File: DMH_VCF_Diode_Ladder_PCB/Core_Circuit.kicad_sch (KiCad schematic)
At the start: 0 parts

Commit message: Main schematic in progress
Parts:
- added C10, C11, C12, C13, C14: 1nF, Capacitor_THT:C_Disc_D4.3mm_W1.9mm_P5.00mm, symbol Device:C
- added C15, C7: 1uF, Capacitor_THT:C_Disc_D4.3mm_W1.9mm_P5.00mm, symbol Device:C
- added D10, D11, D12, D13, D14, D6, D7, D8, D9: 1N4148, Diode_THT:D_DO-35_SOD27_P7.62mm_Horizontal, symbol Diode:1N4148
- added R1, R8: 27k, Resistor_THT:R_Axial_DIN0207_L6.3mm_D2.5mm_P7.62mm_Horizontal, symbol Device:R_US
- added R10, R11, R12, R13, R14, R15, R16, R21: 33k, Resistor_THT:R_Axial_DIN0207_L6.3mm_D2.5mm_P7.62mm_Horizontal, symbol Device:R_US
- added R17, R6: 2k, Resistor_THT:R_Axial_DIN0207_L6.3mm_D2.5mm_P7.62mm_Horizontal, symbol Device:R_US
- added R18, R2, R22, R5, R9: 100k, Resistor_THT:R_Axial_DIN0207_L6.3mm_D2.5mm_P7.62mm_Horizontal, symbol Device:R_US
- added R19, R20, R23: 1k, Resistor_THT:R_Axial_DIN0207_L6.3mm_D2.5mm_P7.62mm_Horizontal, symbol Device:R_US
- added R24, R3, R4: 68k, Resistor_THT:R_Axial_DIN0207_L6.3mm_D2.5mm_P7.62mm_Horizontal, symbol Device:R_US
- added R7: 14k, Resistor_THT:R_Axial_DIN0207_L6.3mm_D2.5mm_P7.62mm_Horizontal, symbol Device:R_US
- added RV1, RV2, RV3, RV4, RV5, RV7: 100k, Potentiometer_THT:Potentiometer_Alpha_RD901F-40-00D_Single_Vertical, symbol Device:R_Potentiometer_US
- added RV6: 50k, Potentiometer_THT:Potentiometer_Bourns_3296W_Vertical, symbol Device:R_Potentiometer_Trim_US
- added U1: TL074, Package_DIP:DIP-14_W7.62mm_Socket, symbol Amplifier_Operational:TL074
- added U2: TL074, symbol Amplifier_Operational:TL074
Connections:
- new net: D6.1 (K), R11.1, R15.1, R8.1, R9.2
- new net: C12.2, D10.2 (A), D9.1 (K), U2.5 (+)
- new net: R2.1, RV2.2
- new net: R2.2, R24.2, R3.2, R4.2, R7.1, U1.9 (-)
- new net: R24.1, RV7.2
- new net: R5.2, R6.2, U1.3 (+)
- new net: R17.1, U1.7
- new net: D7.2 (A), R16.2, R17.2
- new net: R14.2, R15.2, R16.1, U1.6 (-)
- new net: C13.2, D10.1 (K), D11.2 (A)
- new net: D6.2 (A), R7.2, U1.8
- new net: C7.1, RV1.2
- new net: C7.2, R5.1
- new net: C11.2, D8.1 (K), D9.2 (A)
- new net: R1.1, RV2.1
- new net: C10.1, C14.1, D13.1 (K), D14.2 (A), R18.1, U2.1
- new net: C10.2, D7.1 (K), D8.2 (A)
- new net: D13.2 (A), D14.1 (K), R18.2, RV6.1, U2.2 (-)
- new net: RV5.2, U2.3 (+)
- new net: R4.1, RV4.2
- new net: R10.1, R14.1, U1.1, U1.2 (-)
- new net: R10.2, R13.1, U1.13 (-)
- new net: R11.2, R12.2, U1.12 (+)
- new net: R19.1, RV6.2, RV6.3
- new net: C15.2, R22.2, U2.12 (+)
- new net: R23.1, U2.13 (-), U2.14
- new net: C15.1, U2.8
- new net: R20.2, R21.1, U2.9 (-)
- new net: C14.2, D11.1 (K), D12.2 (A)
- new net: D12.1 (K), R13.2, U1.14
- new net: R3.1, RV3.2
- new net: R20.1, RV5.3, U2.6 (-), U2.7
- new net +12V: RV2.3
- new net -12V: R1.2, R9.1
- new net Bus/CV3 Input: RV7.3
- new net CV1 Input: RV3.3
- new net CV2 Input: RV4.3
- new net GND: C11.1, C12.1, C13.1, R12.1, R19.2, R22.1, R6.1, R8.2, RV1.1, RV3.1, RV4.1, RV5.1, RV7.1, U1.10 (+), U1.5 (+), U2.10 (+)
- new net Input: RV1.3
- new net Output: R23.2

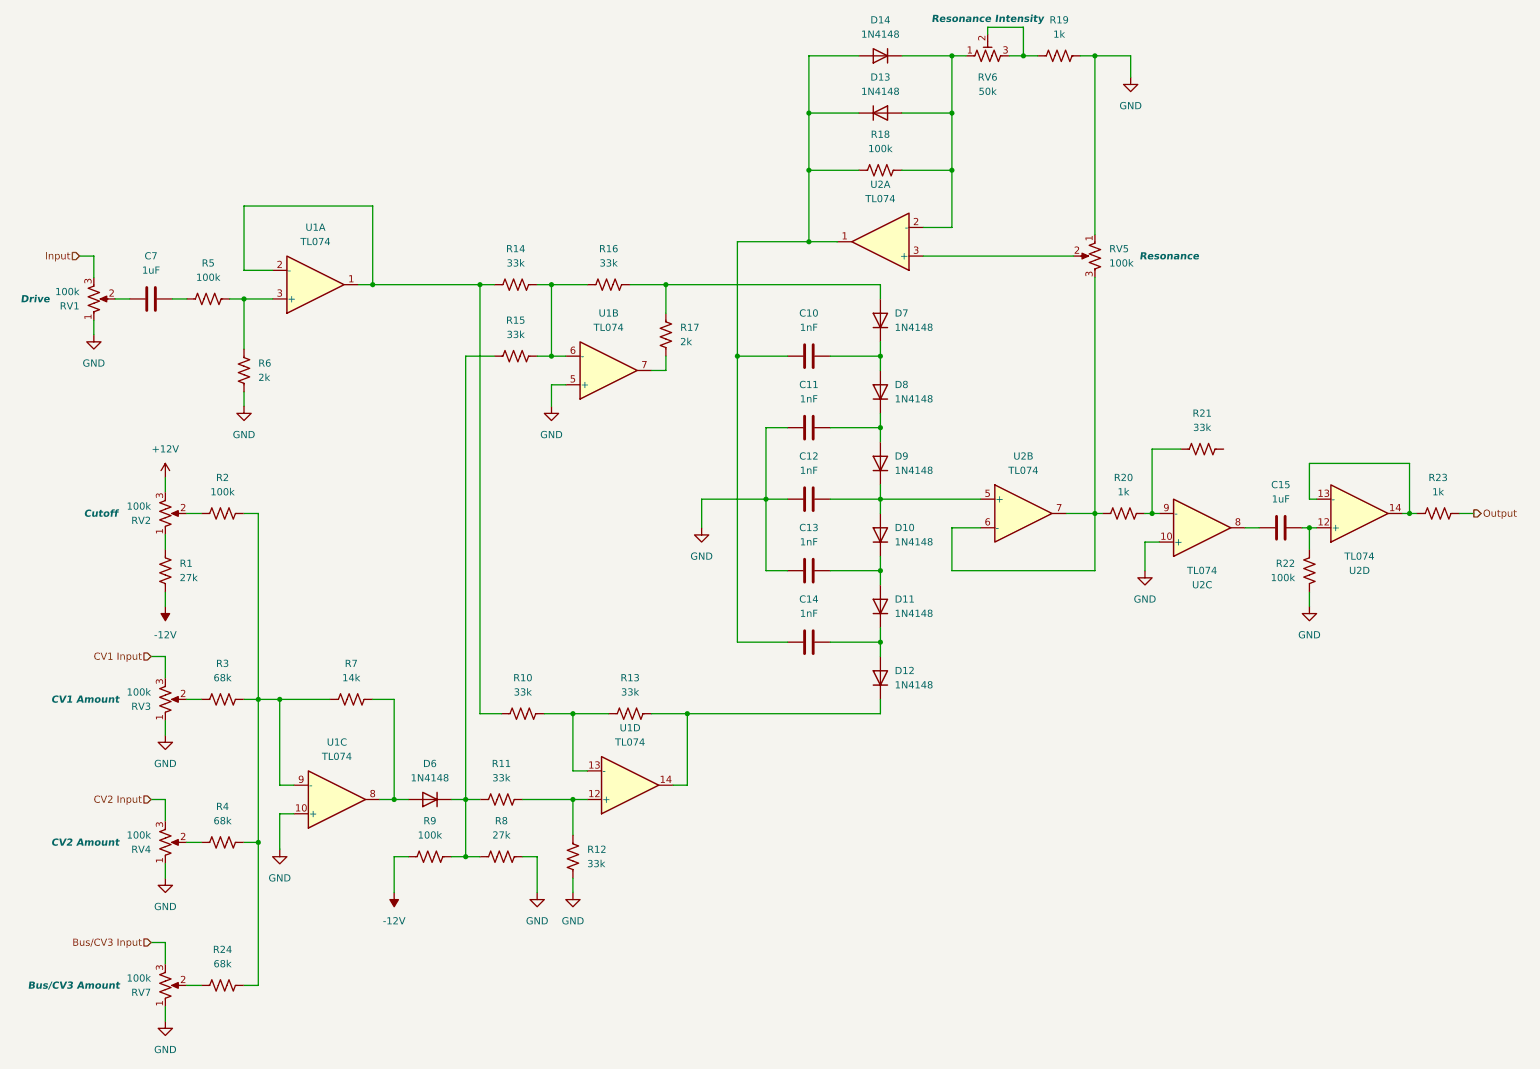
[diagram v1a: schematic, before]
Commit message: Finished schematic and added Bus CV 2 pot
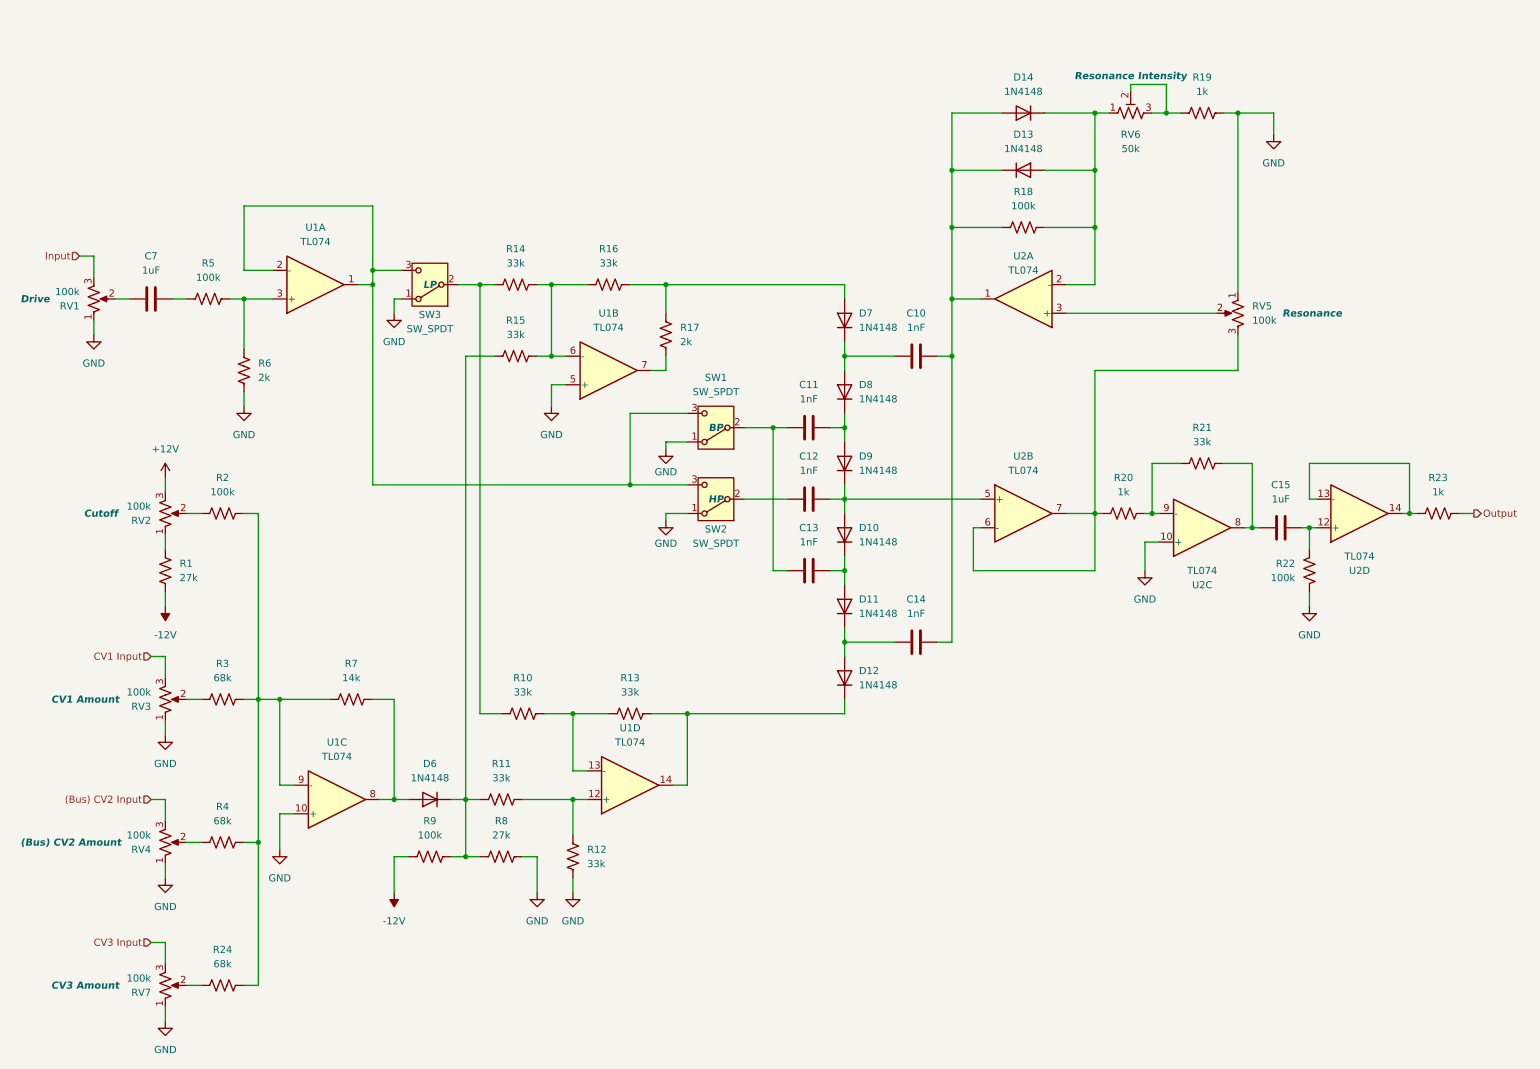
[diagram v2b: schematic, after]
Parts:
- added SW1, SW2, SW3: SW_SPDT, symbol Switch:SW_SPDT
- RV4: Function CV2 Amount -> (Bus) CV2 Amount
- RV7: Function Bus/CV3 Amount -> CV3 Amount
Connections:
- net GND: now also SW1.1 (A), SW2.1 (A), SW3.1 (A); no longer C11.1, C12.1, C13.1
- net at D13.1 (K), D14.2 (A), R18.1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: now also C10.2, C14.2; no longer C10.1, C14.1
- net at D7.1 (K), D8.2 (A): now also C10.1; no longer C10.2
- net at U1.1, U1.2 (-): now also SW1.3 (C), SW2.3 (C), SW3.3 (C); no longer R10.1, R14.1
- net at C15.1, U2.8: now also R21.2
- net at D11.1 (K), D12.2 (A): now also C14.1; no longer C14.2
- net Bus/CV3 Input renamed CV3 Input
- net CV2 Input renamed (Bus) CV2 Input
- new net: C12.1, SW2.2 (B)
- new net: C11.1, C13.1, SW1.2 (B)
- new net: R10.1, R14.1, SW3.2 (B)
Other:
- moved on the sheet: C10, C14, D10, D11, D12, D13, D14, D7, D8, D9, R18, R19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

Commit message: Component placement in progress
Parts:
- RV1, RV2, RV3, RV4, RV5, RV7: footprint Potentiometer_THT:Potentiometer_Alpha_RD901F-40-00D_Single_Vertical -> SynthStuff:Potentiometer_Alpha_RD901F-40-00D_Single_Vertical
- SW1, SW2, SW3: footprint (none) -> SynthStuff:Toggle_Switch_THT
- U2: footprint (none) -> Package_DIP:DIP-14_W7.62mm_Socket
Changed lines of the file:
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@@
 			)
 		)
-		(property "Footprint" ""
+		(property "Footprint" "SynthStuff:Toggle_Switch_THT"
 			(at 135.89 86.36 0)
 			(effects
@@
 			)
 		)
-		(property "Footprint" "Potentiometer_THT:Potentiometer_Alpha_RD901F-40-00D_Single_Vertical"
+		(property "Footprint" "SynthStuff:Potentiometer_Alpha_RD901F-40-00D_Single_Vertical"
 			(at 38.1 101.6 0)
 			(effects
@@
 			)
 		)
-		(property "Footprint" ""
+		(property "Footprint" "Package_DIP:DIP-14_W7.62mm_Socket"
 			(at 191.77 66.04 0)
 			(effects
@@
 			)
 		)
-		(property "Footprint" "Potentiometer_THT:Potentiometer_Alpha_RD901F-40-00D_Single_Vertical"
+		(property "Footprint" "SynthStuff:Potentiometer_Alpha_RD901F-40-00D_Single_Vertical"
 			(at 25.4 63.5 0)
 			(effects
@@
 			)
 		)
-		(property "Footprint" ""
+		(property "Footprint" "SynthStuff:Toggle_Switch_THT"
 			(at 135.89 99.06 0)
 			(effects
@@
 			)
 		)
-		(property "Footprint" "Potentiometer_THT:Potentiometer_Alpha_RD901F-40-00D_Single_Vertical"
+		(property "Footprint" "SynthStuff:Potentiometer_Alpha_RD901F-40-00D_Single_Vertical"
 			(at 38.1 160.02 0)
 			(effects
@@
 			)
 		)
-		(property "Footprint" "Potentiometer_THT:Potentiometer_Alpha_RD901F-40-00D_Single_Vertical"
+		(property "Footprint" "SynthStuff:Potentiometer_Alpha_RD901F-40-00D_Single_Vertical"
 			(at 38.1 134.62 0)
 			(effects
@@
 			)
 		)
-		(property "Footprint" "Potentiometer_THT:Potentiometer_Alpha_RD901F-40-00D_Single_Vertical"
+		(property "Footprint" "SynthStuff:Potentiometer_Alpha_RD901F-40-00D_Single_Vertical"
 			(at 228.6 66.04 0)
 			(effects
@@
 			)
 		)
-		(property "Footprint" ""
+		(property "Footprint" "SynthStuff:Toggle_Switch_THT"
 			(at 85.09 60.96 0)
 			(effects
@@
 			)
 		)
-		(property "Footprint" "Potentiometer_THT:Potentiometer_Alpha_RD901F-40-00D_Single_Vertical"
+		(property "Footprint" "SynthStuff:Potentiometer_Alpha_RD901F-40-00D_Single_Vertical"
 			(at 38.1 185.42 0)
 			(effects

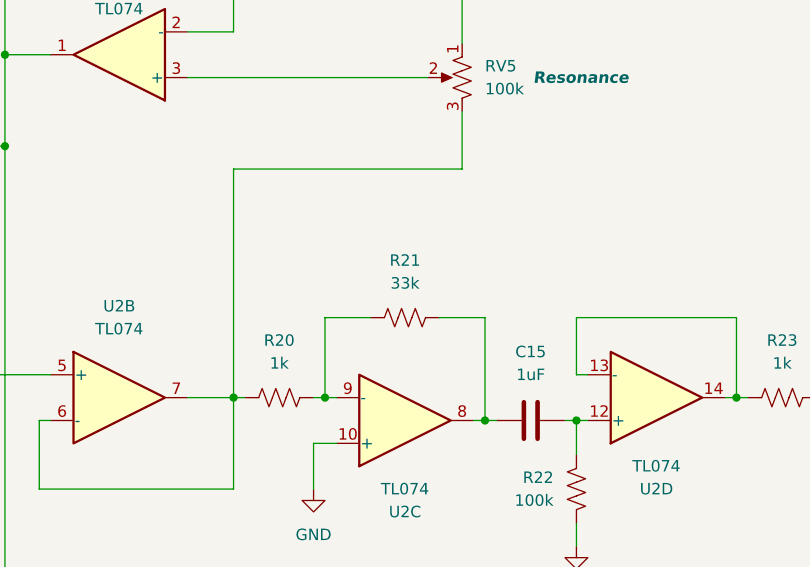
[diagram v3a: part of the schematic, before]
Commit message: Increased output stage gain to x47
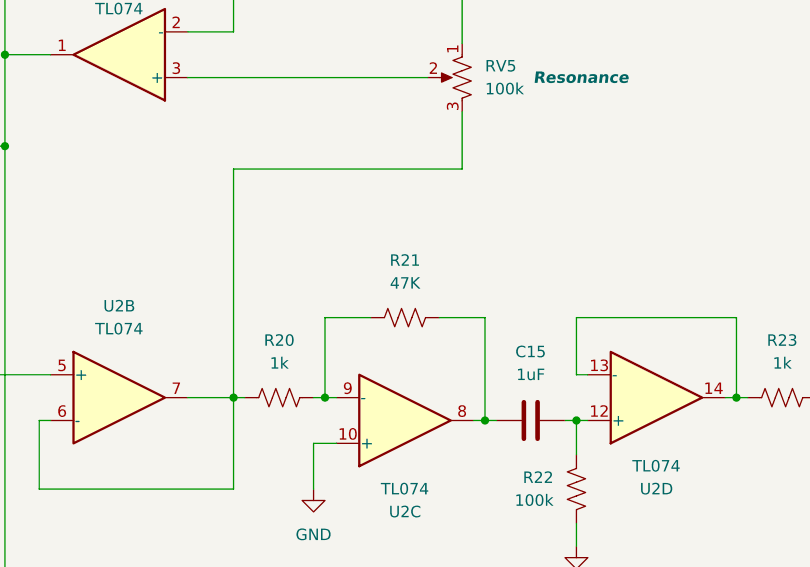
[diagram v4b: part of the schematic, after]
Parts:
- R21: value 33k -> 47K
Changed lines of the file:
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@@
 			)
 		)
-		(property "Value" "33k"
+		(property "Value" "47K"
 			(at 222.25 88.9 90)
 			(effects
